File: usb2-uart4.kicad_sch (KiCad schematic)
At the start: 24 parts, among them U1 CH344Q, U13 TPNUP2202W1T2G, Y1 8MHz

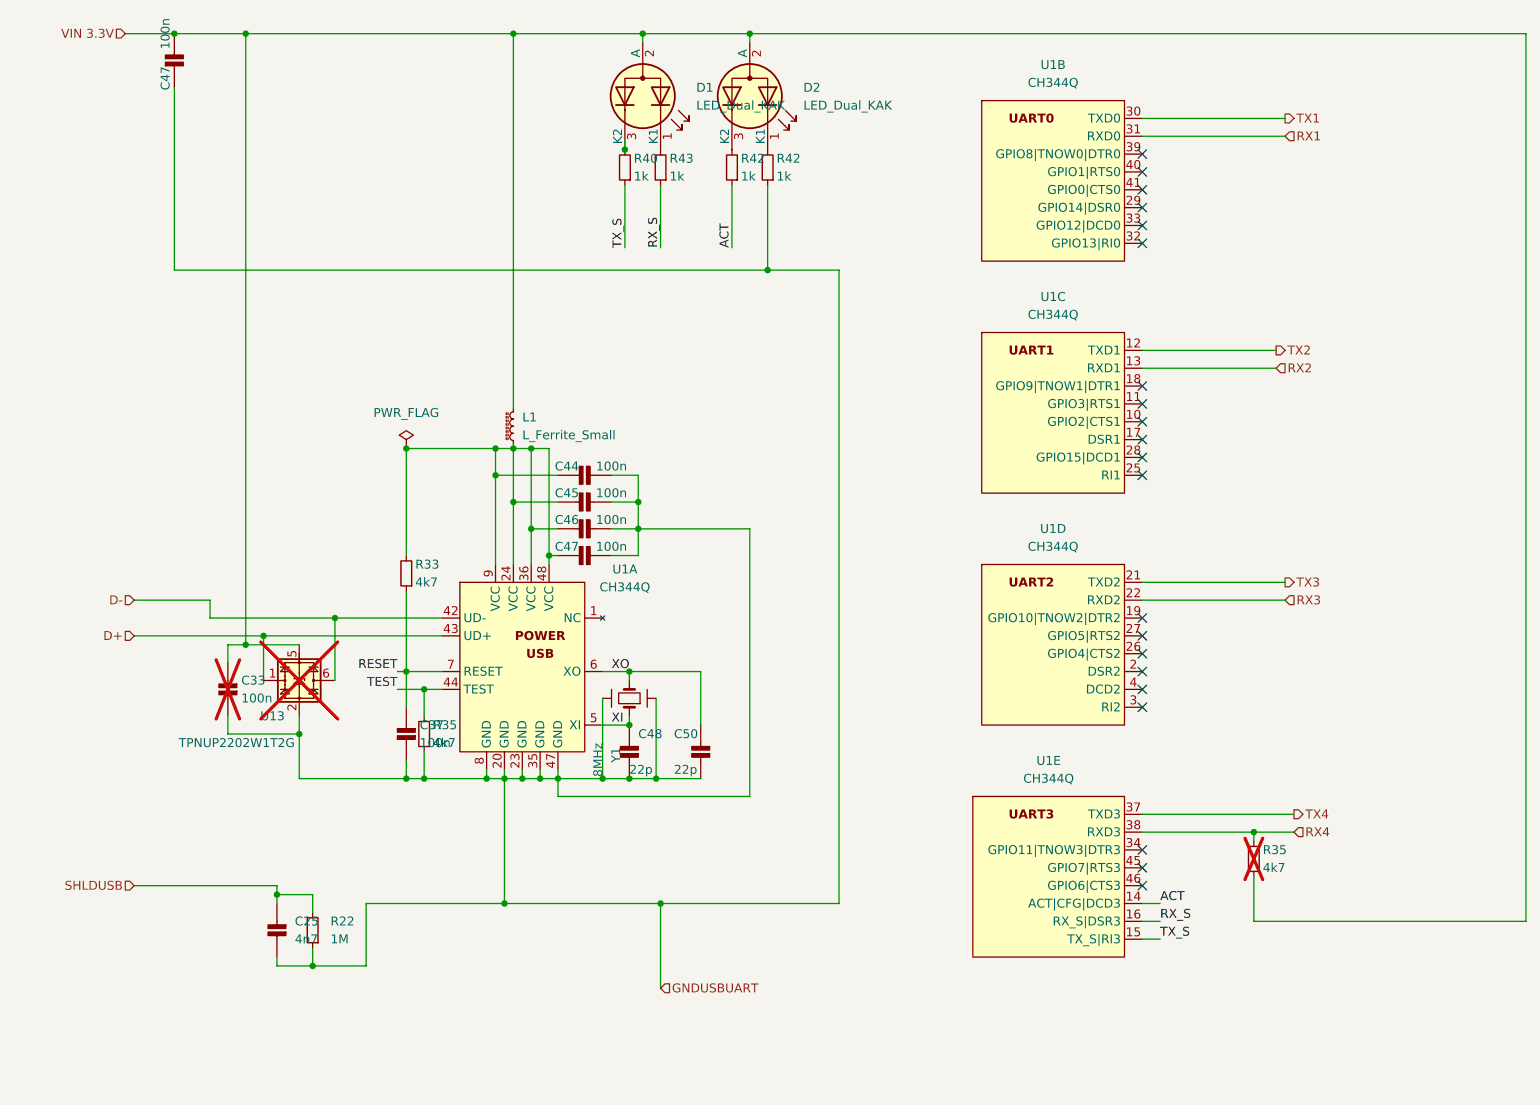
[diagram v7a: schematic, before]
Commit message: Restore 0805 capacitor footprints; Use anotherguse/FuseX copy form isouart4 lib
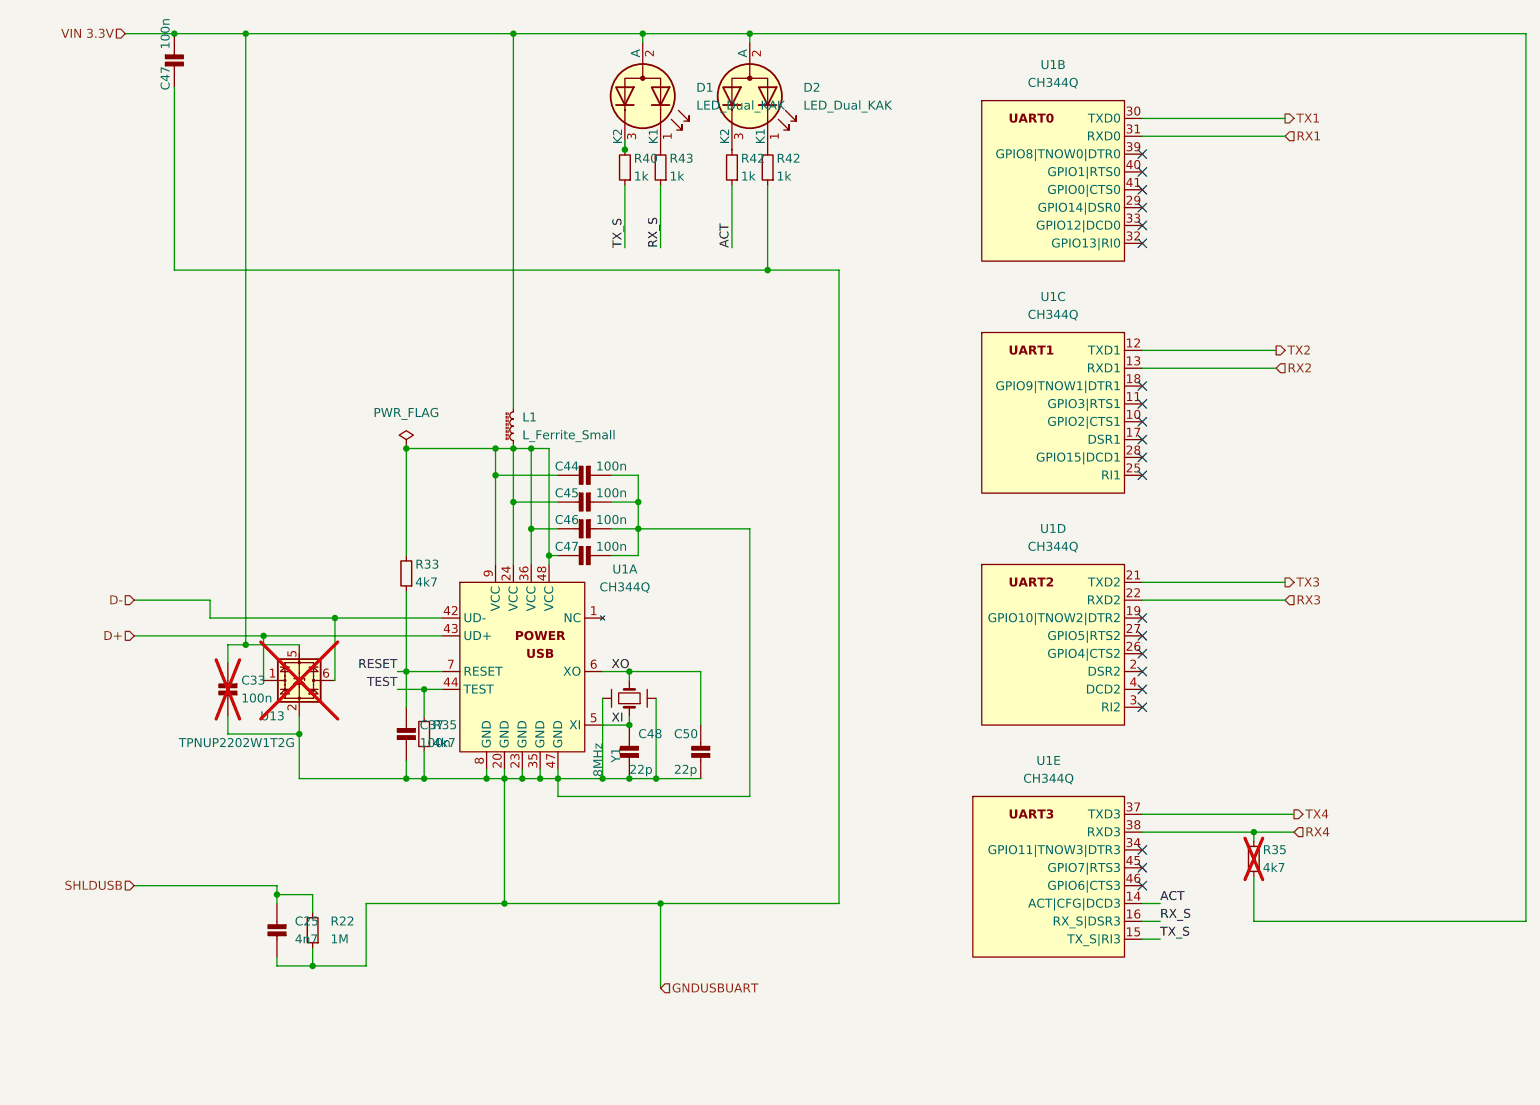
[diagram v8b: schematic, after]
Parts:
- C25, C37, C44, C45, C46, C47, C48, C50: footprint Capacitor_SMD:C_0603_1608Metric_Pad1.08x0.95mm_HandSolder -> Capacitor_SMD:C_0805_2012Metric_Pad1.18x1.45mm_HandSolder
- C33: footprint Capacitor_SMD:C_0603_1608Metric_Pad1.08x0.95mm_HandSolder -> Capacitor_SMD:C_0805_2012Metric_Pad1.18x1.45mm_HandSolder; now left out of the parts list
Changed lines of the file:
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@@
       (effects (font (size 1.27 1.27)))
     )
-    (property "Footprint" "Capacitor_SMD:C_0603_1608Metric_Pad1.08x0.95mm_HandSolder" (at 126.365 85.09 0)
+    (property "Footprint" "Capacitor_SMD:C_0805_2012Metric_Pad1.18x1.45mm_HandSolder" (at 126.365 85.09 0)
       (effects (font (size 1.27 1.27)) hide)
     )
@@
       (effects (font (size 1.27 1.27)) (justify right))
     )
-    (property "Footprint" "Capacitor_SMD:C_0603_1608Metric_Pad1.08x0.95mm_HandSolder" (at 83.82 144.78 0)
+    (property "Footprint" "Capacitor_SMD:C_0805_2012Metric_Pad1.18x1.45mm_HandSolder" (at 83.82 144.78 0)
       (effects (font (size 1.27 1.27)) hide)
     )
@@
       (effects (font (size 1.27 1.27)) (justify right))
     )
-    (property "Footprint" "Capacitor_SMD:C_0603_1608Metric_Pad1.08x0.95mm_HandSolder" (at 102.235 116.84 0)
+    (property "Footprint" "Capacitor_SMD:C_0805_2012Metric_Pad1.18x1.45mm_HandSolder" (at 102.235 116.84 0)
       (effects (font (size 1.27 1.27)) hide)
     )
@@
       (effects (font (size 1.27 1.27)))
     )
-    (property "Footprint" "Capacitor_SMD:C_0603_1608Metric_Pad1.08x0.95mm_HandSolder" (at 69.215 23.495 0)
+    (property "Footprint" "Capacitor_SMD:C_0805_2012Metric_Pad1.18x1.45mm_HandSolder" (at 69.215 23.495 0)
       (effects (font (size 1.27 1.27)) hide)
     )
@@
       (effects (font (size 1.27 1.27)) (justify right))
     )
-    (property "Footprint" "Capacitor_SMD:C_0603_1608Metric_Pad1.08x0.95mm_HandSolder" (at 144.145 119.38 0)
+    (property "Footprint" "Capacitor_SMD:C_0805_2012Metric_Pad1.18x1.45mm_HandSolder" (at 144.145 119.38 0)
       (effects (font (size 1.27 1.27)) hide)
     )
@@
       (effects (font (size 1.27 1.27)))
     )
-    (property "Footprint" "Capacitor_SMD:C_0603_1608Metric_Pad1.08x0.95mm_HandSolder" (at 126.365 81.28 0)
+    (property "Footprint" "Capacitor_SMD:C_0805_2012Metric_Pad1.18x1.45mm_HandSolder" (at 126.365 81.28 0)
       (effects (font (size 1.27 1.27)) hide)
     )
@@
       (effects (font (size 1.27 1.27)))
     )
-    (property "Footprint" "Capacitor_SMD:C_0603_1608Metric_Pad1.08x0.95mm_HandSolder" (at 126.365 88.9 0)
+    (property "Footprint" "Capacitor_SMD:C_0805_2012Metric_Pad1.18x1.45mm_HandSolder" (at 126.365 88.9 0)
       (effects (font (size 1.27 1.27)) hide)
     )
@@
       (effects (font (size 1.27 1.27)))
     )
-    (property "Footprint" "Capacitor_SMD:C_0603_1608Metric_Pad1.08x0.95mm_HandSolder" (at 126.365 92.71 0)
+    (property "Footprint" "Capacitor_SMD:C_0805_2012Metric_Pad1.18x1.45mm_HandSolder" (at 126.365 92.71 0)
       (effects (font (size 1.27 1.27)) hide)
     )
@@
   )
   (symbol (lib_id "isouart4:CAP_NP") (at 76.835 111.76 180) (unit 1)
-    (in_bom yes) (on_board yes) (dnp yes) (fields_autoplaced)
+    (in_bom no) (on_board no) (dnp yes) (fields_autoplaced)
     (property "Reference" "C33" (at 78.74 110.49 0)
       (effects (font (size 1.27 1.27)) (justify right))
@@
       (effects (font (size 1.27 1.27)) (justify right))
     )
-    (property "Footprint" "Capacitor_SMD:C_0603_1608Metric_Pad1.08x0.95mm_HandSolder" (at 76.835 110.49 0)
+    (property "Footprint" "Capacitor_SMD:C_0805_2012Metric_Pad1.18x1.45mm_HandSolder" (at 76.835 110.49 0)
       (effects (font (size 1.27 1.27)) hide)
     )
@@
       (effects (font (size 1.27 1.27)) (justify right))
     )
-    (property "Footprint" "Capacitor_SMD:C_0603_1608Metric_Pad1.08x0.95mm_HandSolder" (at 133.985 119.38 0)
-      (effects (font (size 1.27 1.27)) hide)
-    )
+    (property "Footprint" "Capacitor_SMD:C_0805_2012Metric_Pad1.18x1.45mm_HandSolder" (at 133.985 119.38 0)
+      (effects (font (size 1.27 1.27)) hide)
+    )
